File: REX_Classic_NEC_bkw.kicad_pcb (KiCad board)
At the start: 2 copper layers, 17.8 x 35.6 mm, 9 parts, among them J1 DIP28 legs 27C256, J2 JTAG, J3 PRG, U1 XCR3064-VQ44, U2 29F800BB, U3 LP2980

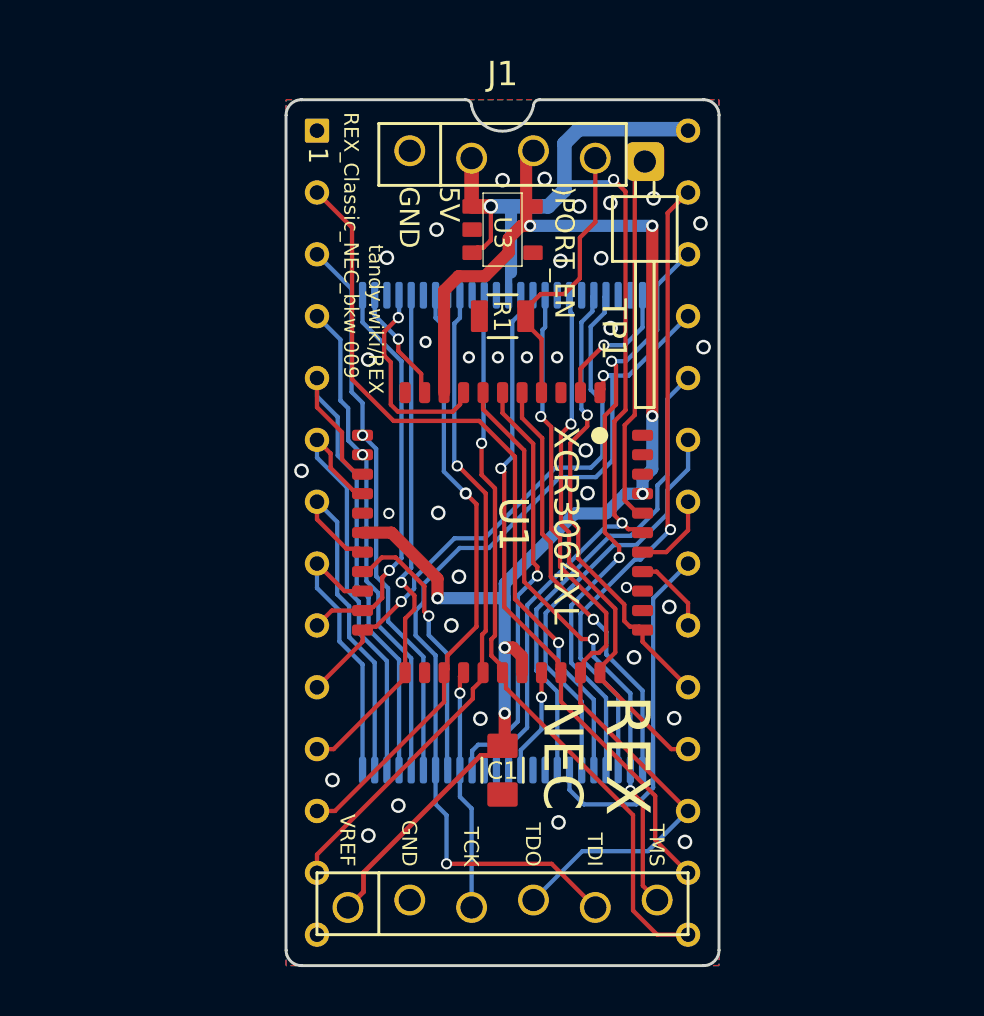
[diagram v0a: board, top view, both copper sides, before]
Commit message: kicad 7, 0.2mm tracks, 0.3x0.5mm vias, add caps on 3v3
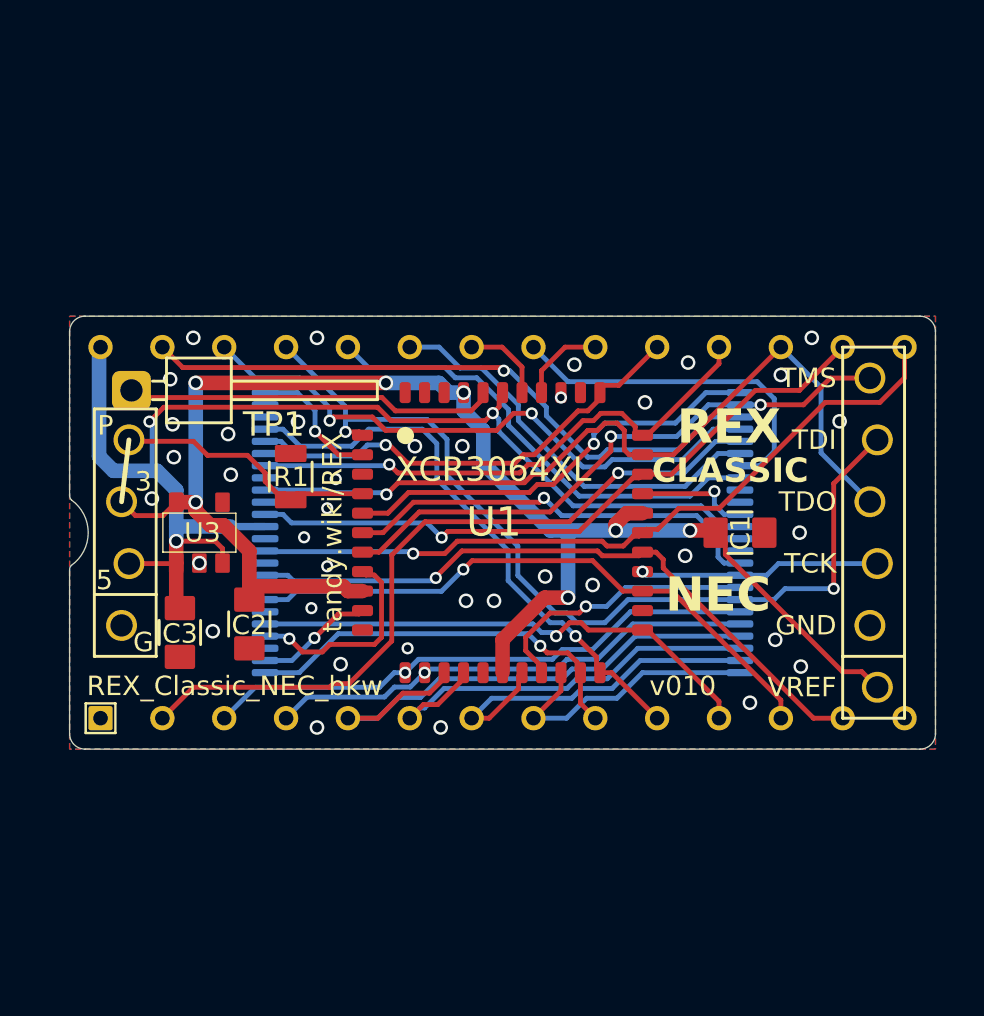
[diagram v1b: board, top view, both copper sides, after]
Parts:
- added C2: 1u, 000_LOCAL:C_0805, F.Cu at (136.8, 102.9)
- added C3: 1u, 000_LOCAL:C_0805, F.Cu at (134.0, 103.3)
- J1: footprint 000_LOCAL:DIP-28_600_pcb -> 000_LOCAL:DIP-28_600_pcb_shallow_notch
- U3: value LP2980 -> LP2980-3.3
- moved TP1 23.1 mm to (132.0, 93.3), turned to 0 degrees
- moved J3 21.9 mm to (131.7, 99.2), turned to 90 degrees
- moved J2 21.6 mm to (162.5, 99.2), turned to 90 degrees
- moved U3 17.6 mm to (134.8, 99.2), turned to 90 degrees
- moved C1 13.8 mm to (157.0, 99.2), turned to 0 degrees
- moved R1 10.9 mm to (138.5, 96.9), turned to -90 degrees
- turned J1 to 90 degrees
- turned U1 to 0 degrees
- turned U2 to 180 degrees
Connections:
- U2 pad 10: (no net) -> unconnected-(U2-NC-Pad10)
- U2 pad 13: (no net) -> unconnected-(U2-NC-Pad13)
- U2 pad 14: (no net) -> unconnected-(U2-NC-Pad14)
- U2 pad 9: (no net) -> unconnected-(U2-NC(A19)-Pad9)
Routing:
- net +5V: track 49.5 -> 51.5 mm
- net +3V3: track 61.0 -> 62.7 mm
- net /PORT_EN: track 11.6 -> 10.9 mm
- net /D5/TDO: track 32.7 -> 33.2 mm
- net GND: vias 35 -> 38
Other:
- board size 17.8 x 35.6 mm -> 35.6 x 17.8 mm
- board text added: "${TITLE}"
- board text added: "3"
- board text added: "3V3"
- board text added: "5"
- board text added: "CLASSIC"
- board text added: "G"
- board text added: "P"
- board text added: "PORT_EN"
- board text added: "R*:${00000000-0000-0000-0000-00005e77bb7a:VALUE} C*:${00000000-0000-0000-0000-00005e77bb27:VALUE} U3:${00000000-0000-0000-0000-00005e77bc2d:VALUE}"
- board text added: "v${REVISION}"
- board text removed: "${TITLE} ${REVISION}"
- board text removed: ")PORT_EN"
- board text removed: "1"
- board text removed: "C1:1uF"
- board text removed: "R1:47K"
- board text removed: "U3:LP2980-3.3"

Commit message: silkscreen
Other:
- board text removed: "XCR3064XL"
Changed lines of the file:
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@@
   (title_block
     (title "REX_Classic_NEC_bkw")
-    (date "2023-07-03")
-    (rev "010")
+    (date "2023-07-04")
+    (rev "011")
     (company "Brian K. White - b.kenyon.w@gmail.com")
     (comment 1 "Based on REX NEC by Steve Adolph")
@@
     (property "ki_keywords" "cap capacitor")
     (attr smd)
-    (fp_text reference "C1" (at 0.0254 0.0004 90) (layer "F.SilkS")
-        (effects (font (size 0.8 0.8) (thickness 0.1)))
+    (fp_text reference "C1" (at 0 0 90) (layer "F.SilkS")
+        (effects (font (size 0.6 0.6) (thickness 0.08)))
     )
     (fp_text value "1u" (at 0 1.75) (layer "F.Fab")
@@
     (property "ki_keywords" "R res resistor")
     (attr smd)
-    (fp_text reference "R1" (at 0.014 -0.01 unlocked) (layer "F.SilkS")
-        (effects (font (size 0.8 0.8) (thickness 0.1)))
+    (fp_text reference "R1" (at 0.05 0 unlocked) (layer "F.SilkS")
+        (effects (font (size 0.6 0.6) (thickness 0.08)))
     )
     (fp_text value "47k" (at 0 1.75 90) (layer "F.Fab")
@@
     (property "ki_keywords" "CPLD")
     (attr smd)
-    (fp_text reference "U1" (at -1.4859 0.2667 unlocked) (layer "F.SilkS")
-        (effects (font (size 1.2065 1.2065) (thickness 0.1016)) (justify left bottom))
+    (fp_text reference "U1" (at 0 -2.794 unlocked) (layer "F.SilkS")
+        (effects (font (size 1 1) (thickness 0.1)))
     )
     (fp_text value "XCR3064-VQ44" (at 0 8) (layer "Dwgs.User") hide
         (effects (font (size 1 1) (thickness 0.1)) (justify bottom))
     )
-    (fp_text user "${REFERENCE}" (at 0 0 -180) (layer "F.Fab")
-        (effects (font (size 1 1) (thickness 0.15)))
+    (fp_text user "${VALUE}" (at 0 0 180) (layer "F.SilkS")
+        (effects (font (size 0.8 0.8) (thickness 0.1)))
     )
     (fp_circle (center -3.9878 -3.9878) (end -3.8116 -3.9878)
@@
     (property "Sheetname" "")
     (attr smd)
-    (fp_text reference "U3" (at 0 0.127 unlocked) (layer "F.SilkS")
+    (fp_text reference "U3" (at -0.05 0) (layer "F.SilkS")
         (effects (font (size 0.8 0.8) (thickness 0.1)))
     )
-    (fp_text value "LP2980-3.3" (at 0 2.9 90) (layer "F.Fab")
-        (effects (font (size 1 1) (thickness 0.15)))
-    )
-    (fp_text user "${REFERENCE}" (at 0 0) (layer "F.Fab")
-        (effects (font (size 0.5 0.5) (thickness 0.075)))
+    (fp_text value "LP2980-3.3" (at 0 2.286 90) (layer "F.SilkS") hide
+        (effects (font (size 0.8 0.8) (thickness 0.1)))
+    )
+    (fp_text user "${REFERENCE}" (at 0 0 180) (layer "F.Fab")
+        (effects (font (size 0.6 0.6) (thickness 0.08)))
     )
     (fp_line (start -0.8 -1.5) (end -0.8 1.5)
-      (stroke (width 0.0508) (type solid)) (layer "F.SilkS"))
+      (stroke (width 0.08) (type solid)) (layer "F.SilkS"))
     (fp_line (start -0.8 1.5) (end 0.8 1.5)
-      (stroke (width 0.0508) (type solid)) (layer "F.SilkS"))
+      (stroke (width 0.08) (type solid)) (layer "F.SilkS"))
     (fp_line (start 0.8 -1.5) (end -0.8 -1.5)
-      (stroke (width 0.0508) (type solid)) (layer "F.SilkS"))
+      (stroke (width 0.08) (type solid)) (layer "F.SilkS"))
     (fp_line (start 0.8 1.5) (end 0.8 -1.5)
-      (stroke (width 0.0508) (type solid)) (layer "F.SilkS"))
+      (stroke (width 0.08) (type solid)) (layer "F.SilkS"))
     (fp_line (start -0.9 -0.9) (end -0.9 1.55)
       (stroke (width 0.1) (type solid)) (layer "F.Fab"))
@@
     (property "ki_keywords" "cap capacitor")
     (attr smd)
-    (fp_text reference "C3" (at 0.05 0 -180) (layer "F.SilkS")
-        (effects (font (size 0.8 0.8) (thickness 0.1)))
+    (fp_text reference "C3" (at 0 0) (layer "F.SilkS")
+        (effects (font (size 0.6 0.6) (thickness 0.08)))
     )
     (fp_text value "1u" (at 0 1.75 90) (layer "F.Fab")
@@
     (property "ki_keywords" "cap capacitor")
     (attr smd)
-    (fp_text reference "C2" (at 0.05 0) (layer "F.SilkS")
-        (effects (font (size 0.8 0.8) (thickness 0.1)))
+    (fp_text reference "C2" (at 0 0 180) (layer "F.SilkS")
+        (effects (font (size 0.6 0.6) (thickness 0.08)))
     )
     (fp_text value "1u" (at 0 1.75 90) (layer "F.Fab")
@@
     (property "Sheetname" "")
     (attr smd)
-    (fp_text reference "U2" (at -1.58496 -0.44958) (layer "B.SilkS") hide
-        (effects (font (size 1.2065 1.2065) (thickness 0.1016)) (justify left bottom mirror))
+    (fp_text reference "U2" (at 0 3.55 unlocked) (layer "B.SilkS")
+        (effects (font (size 1 1) (thickness 0.1)) (justify mirror))
     )
     (fp_text value "29F800BB" (at 0 -0.0004 unlocked) (layer "B.SilkS")
-        (effects (font (size 1.2065 1.2065) (thickness 0.1016)) (justify bottom mirror))
+        (effects (font (size 1 1) (thickness 0.1)) (justify mirror))
     )
     (fp_text user "${REFERENCE}" (at 0 0) (layer "B.Fab")
@@
     (effects (font (size 0.8 0.8) (thickness 0.1)) (justify right))
   )
-  (gr_text "XCR3064XL" (at 142.8238 97.18) (layer "F.SilkS")
-    (effects (font (size 1 1) (thickness 0.1)) (justify left bottom))
-  )
   (gr_text "REX" (at 156.518 94.837) (layer "F.SilkS")

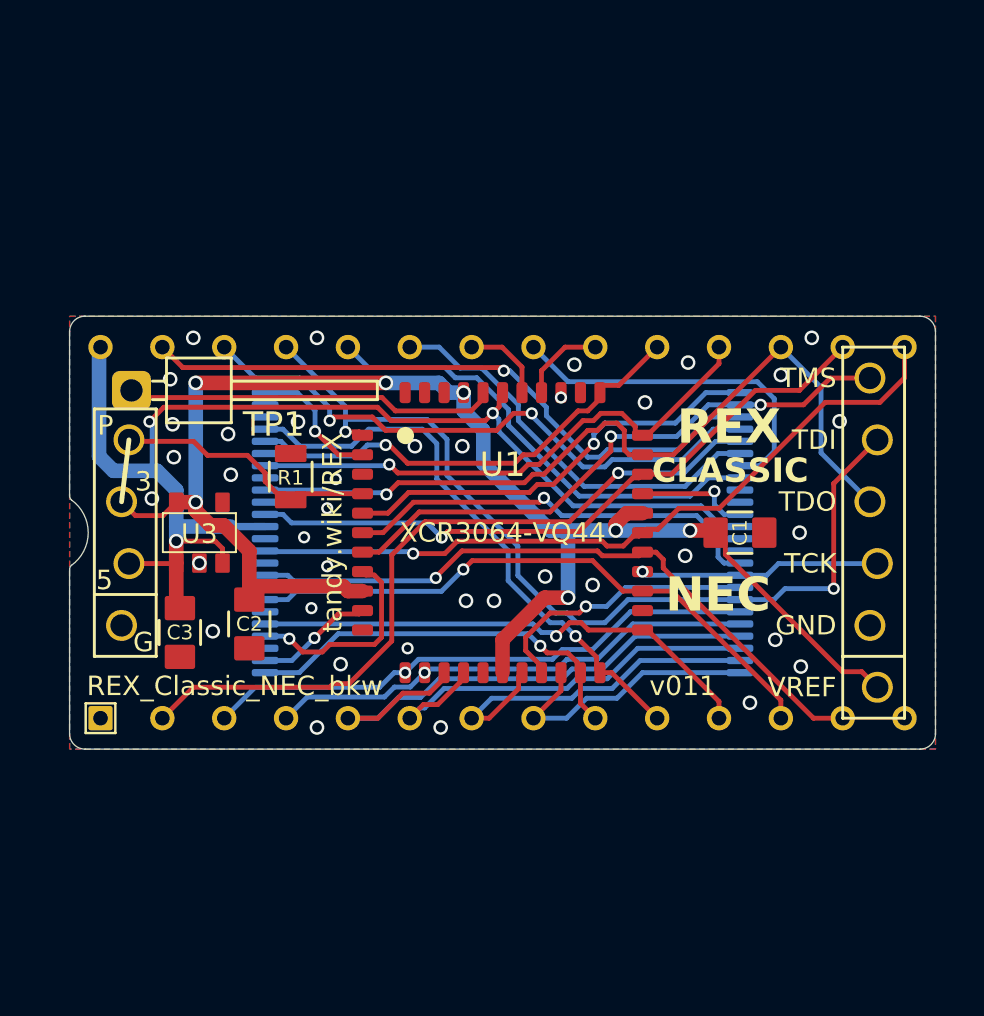
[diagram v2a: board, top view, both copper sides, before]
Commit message: small layout nudges
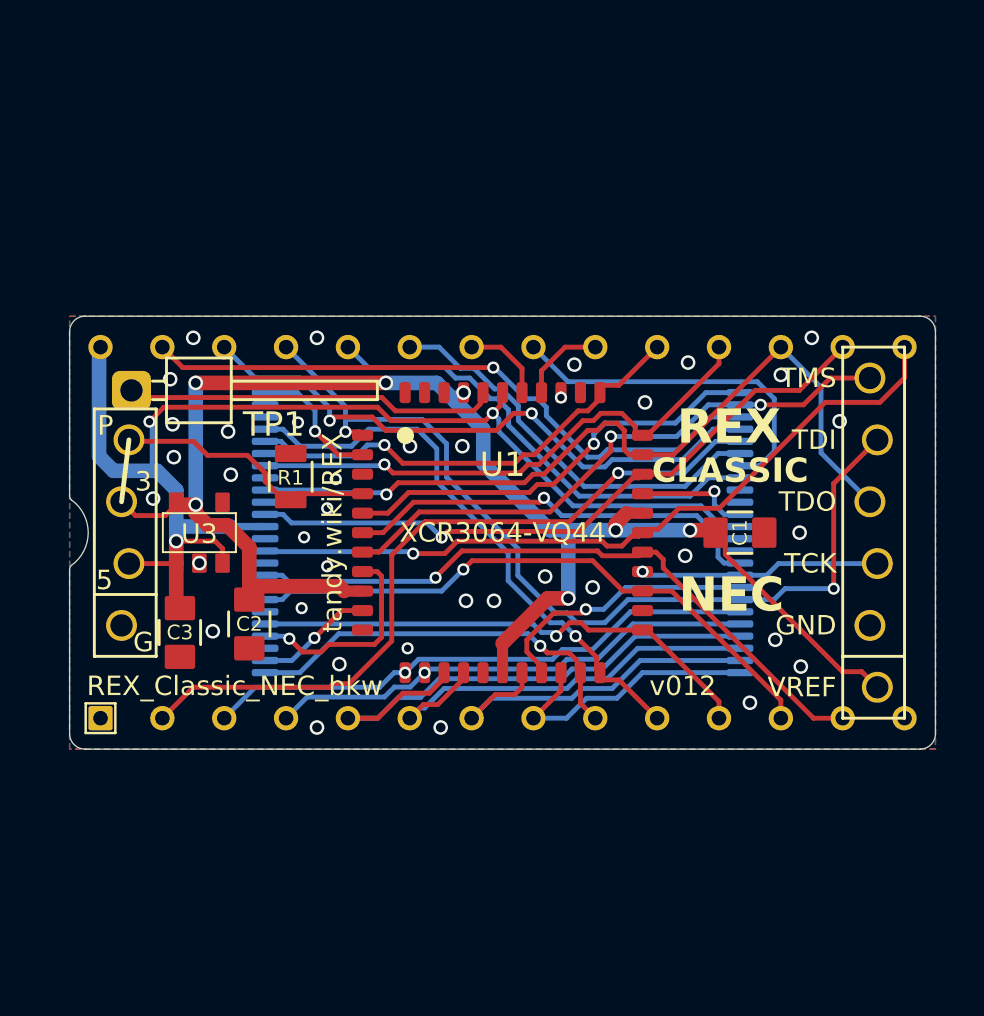
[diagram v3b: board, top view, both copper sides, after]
